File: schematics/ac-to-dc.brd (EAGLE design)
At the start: 30.1 x 21.6 mm, 12 parts, among them IC1 12V

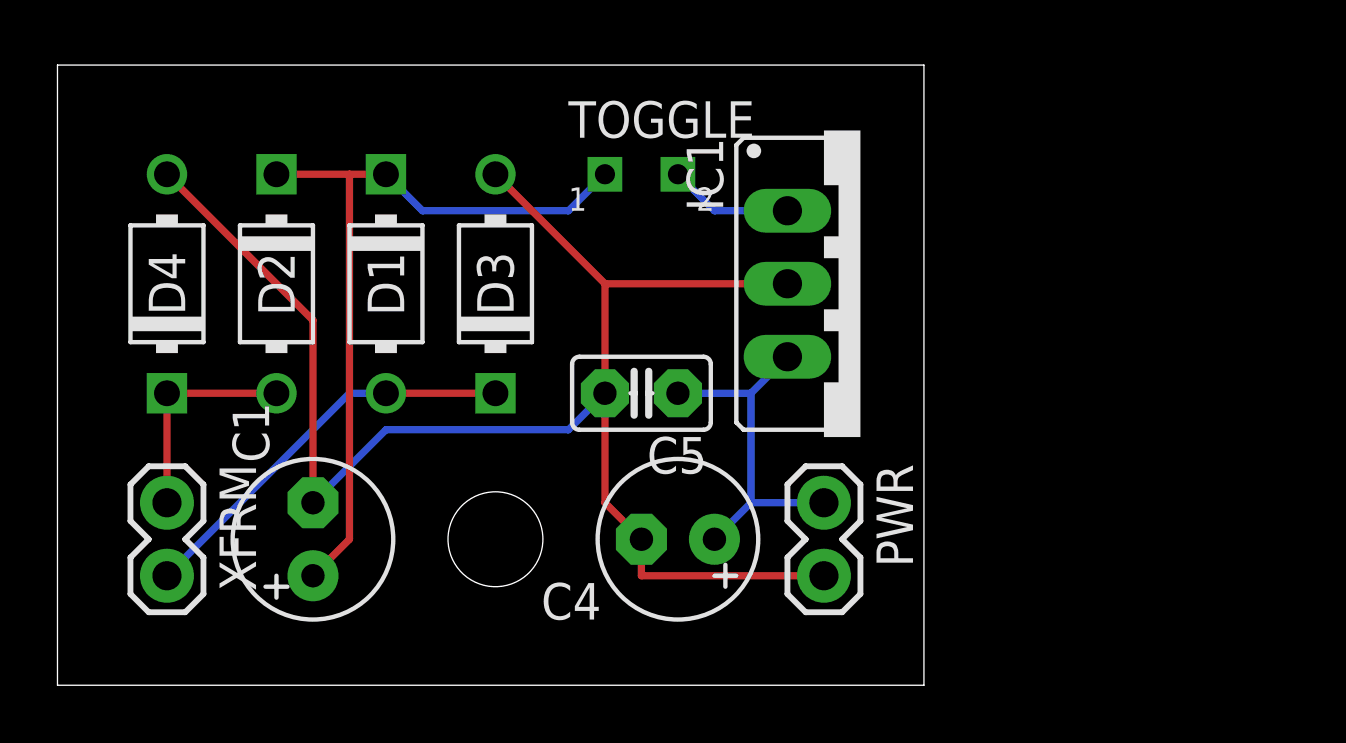
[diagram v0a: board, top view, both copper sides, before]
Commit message: Rethinking the transformer placement
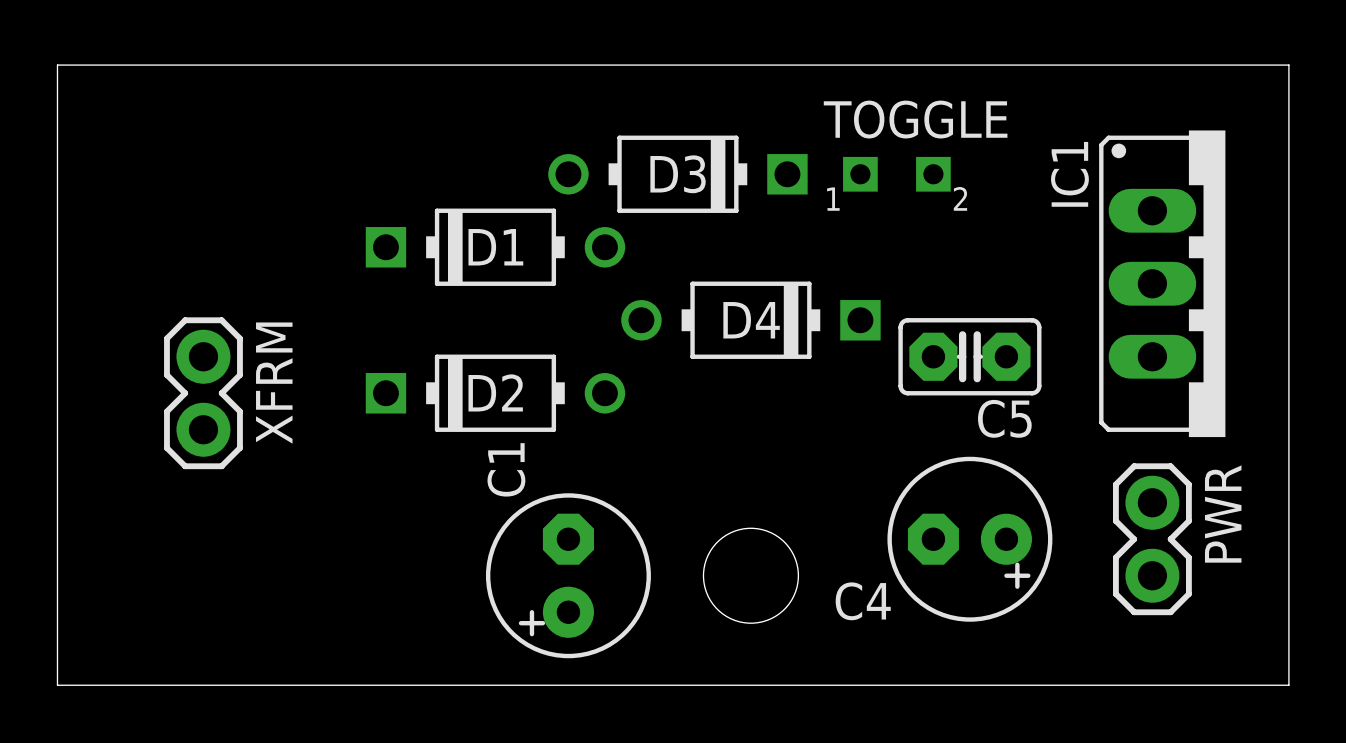
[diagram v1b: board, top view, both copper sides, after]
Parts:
- moved D4 20.4 mm to (24.1, 12.7), turned to 180 degrees
- moved IC1 12.7 mm to (40.6, 14.0)
- moved C5 11.5 mm to (31.8, 11.4)
- moved PWR 11.4 mm to (38.1, 6.35)
- moved C4 10.2 mm to (31.8, 5.08)
- moved C1 8.98 mm to (17.8, 3.81)
- moved JP1 8.98 mm to (24.1, 3.81)
- moved TOGGLE 8.89 mm to (29.2, 17.8)
- moved D2 8.52 mm to (15.2, 10.2), turned to 0 degrees
- moved D3 7.41 mm to (21.6, 17.8), turned to 180 degrees
- moved XFRM 5.24 mm to (5.08, 11.4)
- moved D1 4.02 mm to (15.2, 15.2), turned to 0 degrees
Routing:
- net AGND: track 54.0 -> 0.00 mm
- net N$9: track 27.0 -> 0.00 mm
- net N$2: track 14.1 -> 0.00 mm
- net +12V: track 12.5 -> 0.00 mm
- net N$3: track 7.62 -> 0.00 mm
- net N$1: track 4.34 -> 0.00 mm
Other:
- board size 30.1 x 21.6 mm -> 42.9 x 21.6 mm
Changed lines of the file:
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@@
 <?xml version="1.0" encoding="utf-8"?>
 <!DOCTYPE eagle SYSTEM "eagle.dtd">
-<eagle version="6.1">
+<eagle version="7.4.0">
 <drawing>
 <settings>
@@
 <board>
 <plain>
-<wire x1="0" y1="0" x2="30.15" y2="0" width="0" layer="20"/>
-<wire x1="30.15" y1="0" x2="30.15" y2="21.58" width="0" layer="20"/>
-<wire x1="30.15" y1="21.58" x2="0" y2="21.58" width="0" layer="20"/>
+<wire x1="0" y1="0" x2="42.85" y2="0" width="0" layer="20"/>
+<wire x1="42.85" y1="0" x2="42.85" y2="21.58" width="0" layer="20"/>
+<wire x1="42.85" y1="21.58" x2="0" y2="21.58" width="0" layer="20"/>
 <wire x1="0" y1="21.58" x2="0" y2="0" width="0" layer="20"/>
 </plain>
@@
 </class>
 </classes>
-<designrules>
+<designrules name="default">
 <description language="de">&lt;b&gt;EAGLE Design Rules&lt;/b&gt;
 &lt;p&gt;
@@
 <pass name="Default">
 <param name="RoutingGrid" value="10mil"/>
+<param name="AutoGrid" value="1"/>
+<param name="Efforts" value="0"/>
+<param name="TopRouterVariant" value="1"/>
 <param name="tpViaShape" value="octagon"/>
 <param name="PrefDir.1" value="|"/>
@@
 </autorouter>
 <elements>
-<element name="D1" library="gm-diodes" package="DO41-3" value="1N4001" x="11.43" y="13.97" rot="R270"/>
-<element name="TOGGLE" library="gm-switches" package="SPST" value="SPST" x="20.32" y="17.78"/>
-<element name="D2" library="gm-diodes" package="DO41-3" value="1N4001" x="7.62" y="13.97" rot="R270"/>
-<element name="C4" library="minimidi" package="E2,5-6" value="47uF/25V" x="21.59" y="5.08" rot="R180"/>
-<element name="C5" library="minimidi" package="C025-025X050" value="0.1uF" x="20.32" y="10.16" rot="R180"/>
-<element name="IC1" library="v-reg" package="78XXS" value="12V" x="27.94" y="13.97" rot="R270"/>
-<element name="D3" library="gm-diodes" package="DO41-3" value="1N4001" x="15.24" y="13.97" rot="R90"/>
-<element name="D4" library="gm-diodes" package="DO41-3" value="1N4001" x="3.81" y="13.97" rot="R90"/>
-<element name="C1" library="minimidi" package="E2,5-6" value="47uF/25V" x="8.89" y="5.08" rot="R90"/>
-<element name="XFRM" library="SparkFun" package="1X02" value="" x="3.81" y="6.35" rot="R270"/>
-<element name="PWR" library="SparkFun" package="1X02" value="" x="26.67" y="6.35" rot="R270"/>
-<element name="JP1" library="SparkFun" package="STAND-OFF" value="STAND-OFF" x="15.24" y="5.08"/>
+<element name="D1" library="gm-diodes" package="DO41-3" value="1N4001" x="15.24" y="15.24"/>
+<element name="TOGGLE" library="gm-switches" package="SPST" value="SPST" x="29.21" y="17.78"/>
+<element name="D2" library="gm-diodes" package="DO41-3" value="1N4001" x="15.24" y="10.16"/>
+<element name="C4" library="minimidi" package="E2,5-6" value="47uF/25V" x="31.75" y="5.08" rot="R180"/>
+<element name="C5" library="minimidi" package="C025-025X050" value="0.1uF" x="31.75" y="11.43" rot="R180"/>
+<element name="IC1" library="v-reg" package="78XXS" value="12V" x="40.64" y="13.97" rot="R270"/>
+<element name="D3" library="gm-diodes" package="DO41-3" value="1N4001" x="21.59" y="17.78" rot="R180"/>
+<element name="D4" library="gm-diodes" package="DO41-3" value="1N4001" x="24.13" y="12.7" rot="R180"/>
+<element name="C1" library="minimidi" package="E2,5-6" value="47uF/25V" x="17.78" y="3.81" rot="R90"/>
+<element name="XFRM" library="SparkFun" package="1X02" value="" x="5.08" y="11.43" rot="R270"/>
+<element name="PWR" library="SparkFun" package="1X02" value="" x="38.1" y="6.35" rot="R270"/>
+<element name="JP1" library="SparkFun" package="STAND-OFF" value="STAND-OFF" x="24.13" y="3.81"/>
 </elements>
 <signals>
@@
 <contactref element="D3" pad="C"/>
 <contactref element="XFRM" pad="2"/>
-<wire x1="15.24" y1="10.16" x2="11.43" y2="10.16" width="0.254" layer="1"/>
-<wire x1="10.16" y1="10.16" x2="3.81" y2="3.81" width="0.254" layer="16"/>
-<wire x1="11.43" y1="10.16" x2="10.16" y2="10.16" width="0.254" layer="16"/>
+<wire x1="19.05" y1="15.24" x2="25.4" y2="17.78" width="0" layer="19" extent="1-1"/>
+<wire x1="5.08" y1="8.89" x2="19.05" y2="15.24" width="0" layer="19" extent="1-1"/>
 </signal>
 <signal name="N$9">
@@
 <contactref element="D2" pad="C"/>
 <contactref element="C1" pad="+"/>
-<wire x1="17.78" y1="16.51" x2="19.05" y2="17.78" width="0.254" layer="16"/>
-<wire x1="12.7" y1="16.51" x2="17.78" y2="16.51" width="0.254" layer="16"/>
-<wire x1="11.43" y1="17.78" x2="12.7" y2="16.51" width="0.254" layer="16"/>
-<wire x1="11.43" y1="17.78" x2="10.16" y2="17.78" width="0.254" layer="1"/>
-<wire x1="10.16" y1="17.78" x2="7.62" y2="17.78" width="0.254" layer="1"/>
-<wire x1="10.16" y1="5.08" x2="8.89" y2="3.81" width="0.254" layer="1"/>
-<wire x1="10.16" y1="17.78" x2="10.16" y2="5.08" width="0.254" layer="1"/>
+<wire x1="11.43" y1="15.24" x2="27.94" y2="17.78" width="0" layer="19" extent="1-1"/>
+<wire x1="11.43" y1="10.16" x2="11.43" y2="15.24" width="0" layer="19" extent="1-1"/>
+<wire x1="17.78" y1="2.54" x2="11.43" y2="10.16" width="0" layer="19" extent="1-1"/>
 </signal>
 <signal name="+12V">
@@
 <contactref element="IC1" pad="OUT"/>
 <contactref element="PWR" pad="1"/>
-<wire x1="24.13" y1="10.16" x2="25.4" y2="11.43" width="0.254" layer="16"/>
-<wire x1="21.59" y1="10.16" x2="24.13" y2="10.16" width="0.254" layer="16"/>
-<wire x1="24.13" y1="6.35" x2="22.86" y2="5.08" width="0.254" layer="16"/>
-<wire x1="26.67" y1="6.35" x2="24.13" y2="6.35" width="0.254" layer="16"/>
-<wire x1="24.13" y1="6.35" x2="24.13" y2="10.16" width="0.254" layer="16"/>
+<wire x1="33.02" y1="11.43" x2="38.1" y2="11.43" width="0" layer="19" extent="1-1"/>
+<wire x1="38.1" y1="6.35" x2="38.1" y2="11.43" width="0" layer="19" extent="1-1"/>
+<wire x1="33.02" y1="5.08" x2="38.1" y2="6.35" width="0" layer="19" extent="1-1"/>
 </signal>
 <signal name="AGND">
@@
 <contactref element="IC1" pad="GND"/>
 <contactref element="PWR" pad="2"/>
-<wire x1="8.89" y1="12.7" x2="3.81" y2="17.78" width="0.254" layer="1"/>
-<wire x1="8.89" y1="6.35" x2="8.89" y2="12.7" width="0.254" layer="1"/>
-<wire x1="19.05" y1="13.97" x2="15.24" y2="17.78" width="0.254" layer="1"/>
-<wire x1="19.05" y1="10.16" x2="19.05" y2="13.97" width="0.254" layer="1"/>
-<wire x1="19.05" y1="13.97" x2="25.4" y2="13.97" width="0.254" layer="1"/>
-<wire x1="19.05" y1="6.35" x2="20.32" y2="5.08" width="0.254" layer="1"/>
-<wire x1="19.05" y1="10.16" x2="19.05" y2="6.35" width="0.254" layer="1"/>
-<wire x1="20.32" y1="3.81" x2="26.67" y2="3.81" width="0.254" layer="1"/>
-<wire x1="20.32" y1="5.08" x2="20.32" y2="3.81" width="0.254" layer="1"/>
-<wire x1="11.43" y1="8.89" x2="8.89" y2="6.35" width="0.254" layer="16"/>
-<wire x1="17.78" y1="8.89" x2="11.43" y2="8.89" width="0.254" layer="16"/>
-<wire x1="19.05" y1="10.16" x2="17.78" y2="8.89" width="0.254" layer="16"/>
+<wire x1="30.48" y1="11.43" x2="38.1" y2="13.97" width="0" layer="19" extent="1-1"/>
+<wire x1="30.48" y1="5.08" x2="30.48" y2="11.43" width="0" layer="19" extent="1-1"/>
+<wire x1="38.1" y1="3.81" x2="30.48" y2="5.08" width="0" layer="19" extent="1-1"/>
+<wire x1="20.32" y1="12.7" x2="30.48" y2="11.43" width="0" layer="19" extent="1-1"/>
+<wire x1="17.78" y1="17.78" x2="20.32" y2="12.7" width="0" layer="19" extent="1-1"/>
+<wire x1="17.78" y1="5.08" x2="20.32" y2="12.7" width="0" layer="19" extent="1-1"/>
 </signal>
 <signal name="N$3">
@@
 <contactref element="D2" pad="A"/>
 <contactref element="XFRM" pad="1"/>
-<wire x1="7.62" y1="10.16" x2="3.81" y2="10.16" width="0.254" layer="1"/>
-<wire x1="3.81" y1="10.16" x2="3.81" y2="6.35" width="0.254" layer="1"/>
+<wire x1="19.05" y1="10.16" x2="27.94" y2="12.7" width="0" layer="19" extent="1-1"/>
+<wire x1="5.08" y1="11.43" x2="19.05" y2="10.16" width="0" layer="19" extent="1-1"/>
 </signal>
 <signal name="N$1">
 <contactref element="IC1" pad="IN"/>
 <contactref element="TOGGLE" pad="2"/>
-<wire x1="22.86" y1="16.51" x2="21.59" y2="17.78" width="0.254" layer="16"/>
-<wire x1="25.4" y1="16.51" x2="22.86" y2="16.51" width="0.254" layer="16"/>
+<wire x1="30.48" y1="17.78" x2="38.1" y2="16.51" width="0" layer="19" extent="1-1"/>
 </signal>
 </signals>

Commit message: Reworked the boards
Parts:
- moved D4 19.4 mm to (5.08, 8.89), turned to 0 degrees
- moved C4 18.5 mm to (14.0, 10.2)
- moved C5 18.5 mm to (14.0, 16.5)
- moved IC1 17.8 mm to (22.9, 14.0)
- moved D3 17.3 mm to (5.08, 12.7)
- moved PWR 16.6 mm to (21.6, 5.08)
- moved TOGGLE 15.5 mm to (14.0, 20.3)
- moved D2 12.0 mm to (5.08, 16.5), turned to 180 degrees
- moved D1 11.4 mm to (5.08, 20.3), turned to 180 degrees
- moved XFRM 9.25 mm to (2.54, 2.54), turned to 0 degrees
- moved C1 7.62 mm to (10.2, 3.81), turned to 0 degrees
- moved JP1 7.62 mm to (16.5, 3.81)
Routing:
- net AGND: track 0.00 -> 44.9 mm
- net N$2: track 0.00 -> 22.6 mm
- net N$9: track 0.00 -> 21.3 mm
- net +12V: track 0.00 -> 18.1 mm
- net N$3: track 0.00 -> 15.6 mm
- net N$1: track 0.00 -> 6.71 mm
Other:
- board size 42.9 x 21.6 mm -> 23.8 x 21.6 mm
